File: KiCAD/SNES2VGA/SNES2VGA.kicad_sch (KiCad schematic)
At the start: 16 parts, among them J1 3.5mm_vertical, P1 AVMulti_Main, P2 VGA

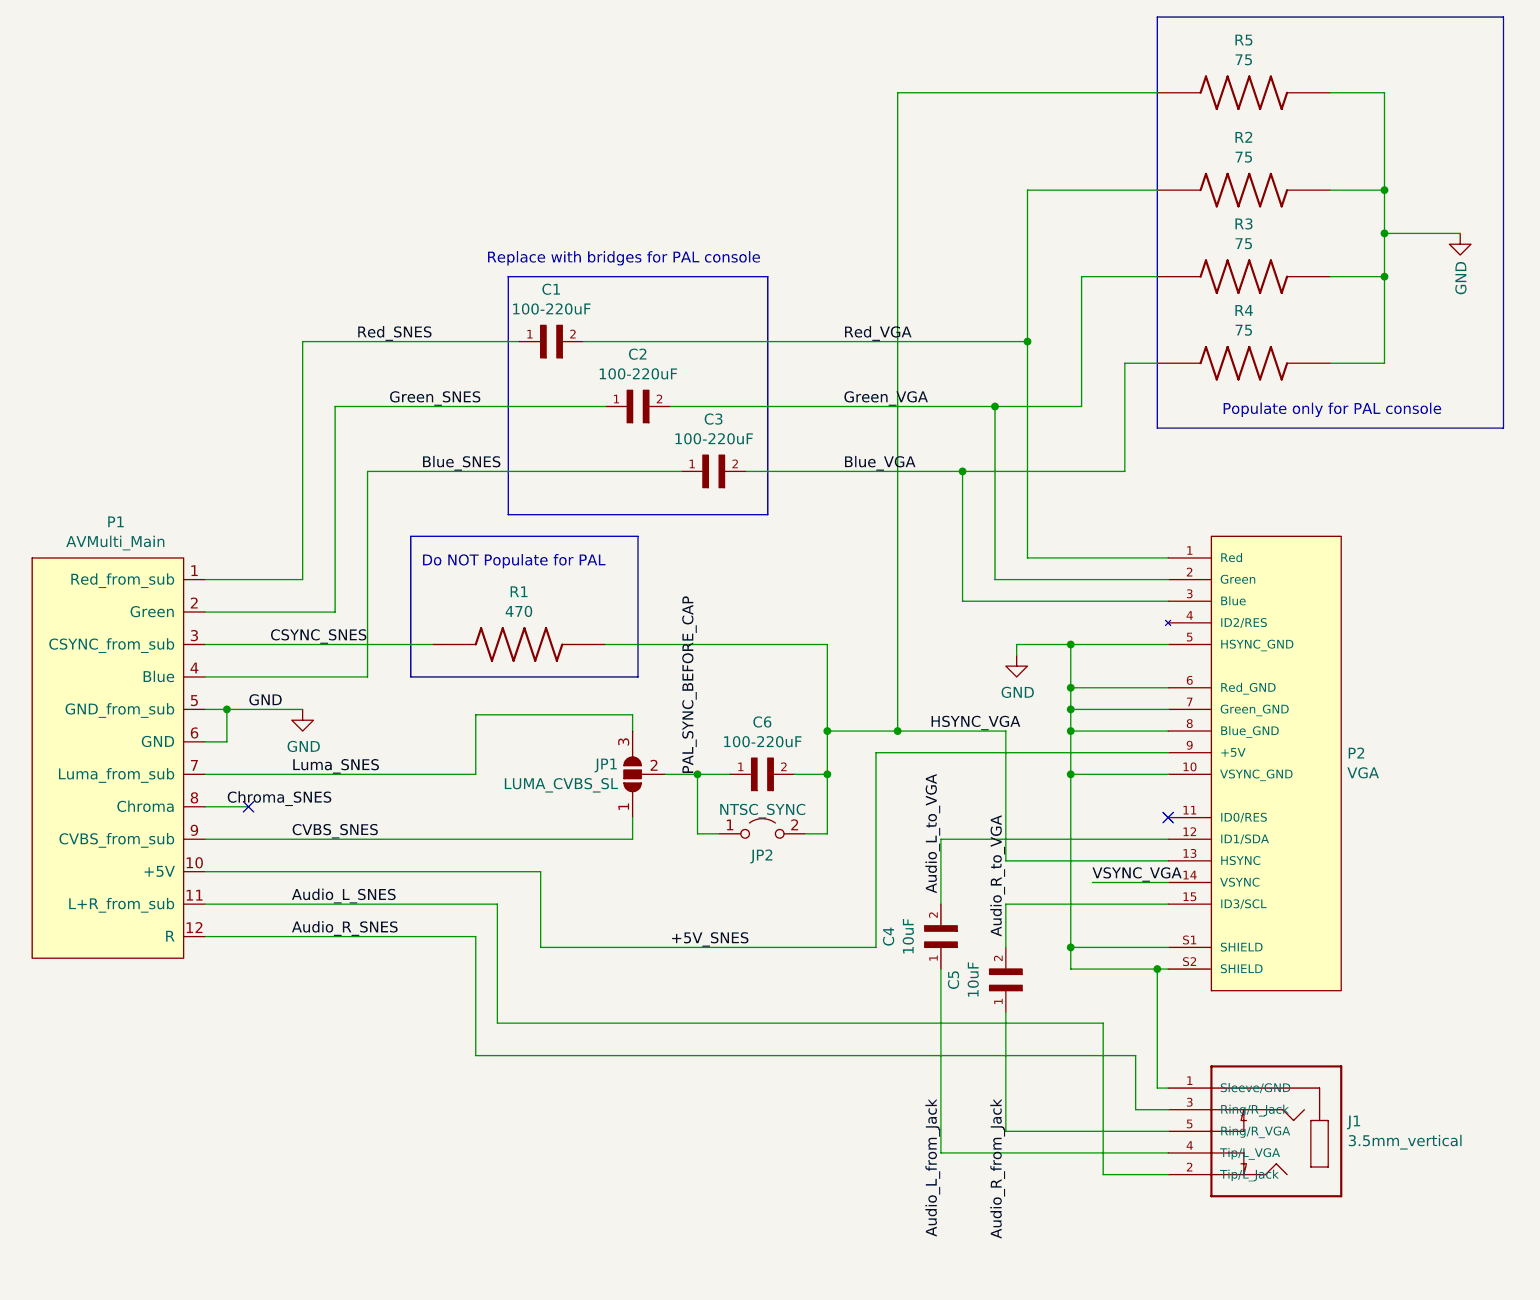
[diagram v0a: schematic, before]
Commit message: Update to KiCad 9
 - Use kicad symbols and footprints if possible
 - Add JLCPCB QR/number placement square/text
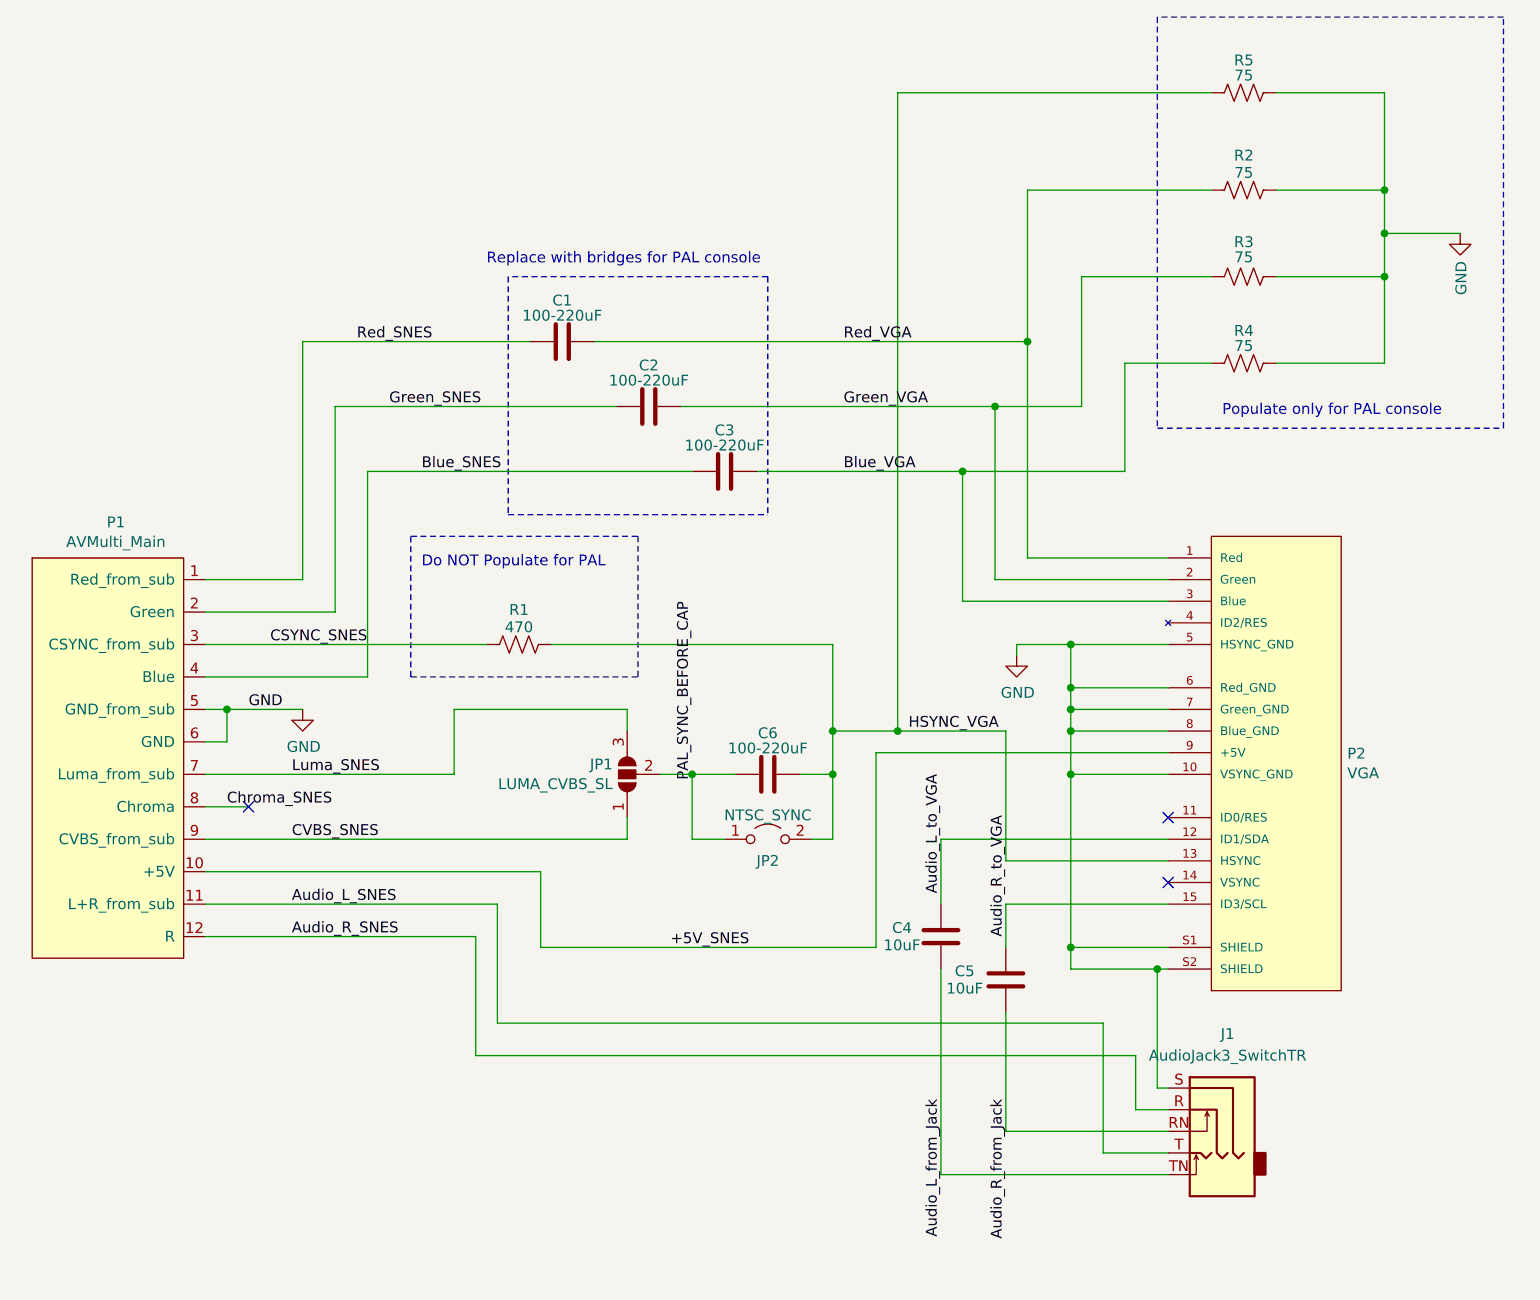
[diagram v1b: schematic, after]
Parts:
- removed J1: 3.5mm_vertical, SNES2VGA_Library:3.5mm_vertical, symbol SNES2VGA_Library:3.5mm_vertical
- added J1: AudioJack3_SwitchTR, Connector_Audio:Jack_3.5mm_CUI_SJ1-3535NG_Horizontal, symbol Connector_Audio:AudioJack3_SwitchTR
- C1, C2, C3, C6: footprint SNES2VGA_Library:Cap_SMD_1206 -> Capacitor_SMD:C_1206_3216Metric; symbol SNES2VGA_Library:Cap_SMD_1206 -> Device:C
- C4, C5: footprint SNES2VGA_Library:Cap_SMD_0603 -> Capacitor_SMD:C_0603_1608Metric; symbol SNES2VGA_Library:Cap_0603 -> Device:C
- JP1: footprint SNES2VGA_Library:SolderJumper-3_P1.3mm_Open_RoundedPad1.0x1.5mm -> Jumper:SolderJumper-3_P1.3mm_Open_RoundedPad1.0x1.5mm; now left out of the parts list
- JP2: now left out of the parts list
- R1, R2, R3, R4, R5: footprint SNES2VGA_Library:Resistor_SMD_0603 -> Resistor_SMD:R_0603_1608Metric; symbol SNES2VGA_Library:Resistor_0603 -> Device:R_US
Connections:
- net Audio_L_SNES: now also J1.T
- net Audio_L_from_Jack: now also C4.2, J1.TN; no longer C4.1
- net Audio_L_to_VGA: now also C4.1; no longer C4.2
- net Audio_R_SNES: now also J1.R
- net Audio_R_from_Jack: now also C5.2, J1.RN; no longer C5.1
- net Audio_R_to_VGA: now also C5.1; no longer C5.2
- net GND: now also J1.S
- net VSYNC_VGA: no longer names the net of P2.14 (VSYNC)
- no-connect marks 2 -> 3
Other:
- moved on the sheet: JP1, JP2

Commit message: Add part information for Digikey and Mfg#
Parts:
- C1, C2, C3, C6: Digikey Product Number (none) -> 490-GRM31CR60J227ME11KCT-ND; Manufacturer Product Number (none) -> GRM31CR60J227ME11K
- C4, C5: Digikey Product Number (none) -> 1276-1119-1-ND; Manufacturer Product Number (none) -> CL10A106MQ8NNNC
- R1: Digikey Product Number (none) -> 311-470HRCT-ND; Manufacturer Product Number (none) -> RC0603FR-07470RL
- R2, R3, R4, R5: Digikey Product Number (none) -> 13-RC0603FR-1075RLCT-ND; Manufacturer Product Number (none) -> RC0603FR-1075RL
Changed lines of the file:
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@@
 			)
 		)
-		(property "Datasheet" "~"
+		(property "Datasheet" "https://mm.digikey.com/Volume0/opasdata/d220001/medias/docus/609/CL10A106MQ8NNNC_Spec.pdf"
 			(at 162.56 121.92 0)
 			(effects
@@
 			)
 		)
+		(property "Digikey Product Number" "1276-1119-1-ND"
+			(at 162.56 121.92 0)
+			(effects
+				(font
+					(size 1.27 1.27)
+				)
+				(hide yes)
+			)
+		)
+		(property "Manufacturer Product Number" "CL10A106MQ8NNNC"
+			(at 162.56 121.92 0)
+			(effects
+				(font
+					(size 1.27 1.27)
+				)
+				(hide yes)
+			)
+		)
 		(pin "1"
 		)
@@
 			)
 		)
-		(property "Datasheet" "~"
+		(property "Datasheet" "https://mm.digikey.com/Volume0/opasdata/d220001/medias/docus/609/CL10A106MQ8NNNC_Spec.pdf"
 			(at 170.18 127 0)
 			(effects
@@
 			)
 		)
+		(property "Digikey Product Number" "1276-1119-1-ND"
+			(at 170.18 127 0)
+			(effects
+				(font
+					(size 1.27 1.27)
+				)
+				(hide yes)
+			)
+		)
+		(property "Manufacturer Product Number" "CL10A106MQ8NNNC"
+			(at 170.18 127 0)
+			(effects
+				(font
+					(size 1.27 1.27)
+				)
+				(hide yes)
+			)
+		)
 		(pin "1"
 		)
@@
 			)
 		)
-		(property "Datasheet" "~"
+		(property "Datasheet" "https://www.yageo.com/upload/media/product/products/datasheet/rchip/PYu-RC_Group_51_RoHS_L_12.pdf"
 			(at 113.03 87.63 0)
 			(effects
@@
 		)
 		(property "Description" "Resistor, US symbol"
+			(at 113.03 87.63 0)
+			(effects
+				(font
+					(size 1.27 1.27)
+				)
+				(hide yes)
+			)
+		)
+		(property "Digikey Product Number" "311-470HRCT-ND"
+			(at 113.03 87.63 0)
+			(effects
+				(font
+					(size 1.27 1.27)
+				)
+				(hide yes)
+			)
+		)
+		(property "Manufacturer Product Number" "RC0603FR-07470RL"
 			(at 113.03 87.63 0)
 			(effects
@@
 			)
 		)
-		(property "Datasheet" "~"
+		(property "Datasheet" "https://search.murata.co.jp/Ceramy/image/img/A01X/G101/ENG/GRM31CR60J227ME11-01A.pdf"
 			(at 118.11 52.07 0)
 			(effects
@@
 		)
 		(property "Description" "Unpolarized capacitor"
+			(at 118.11 52.07 0)
+			(effects
+				(font
+					(size 1.27 1.27)
+				)
+				(hide yes)
+			)
+		)
+		(property "Digikey Product Number" "490-GRM31CR60J227ME11KCT-ND"
+			(at 118.11 52.07 0)
+			(effects
+				(font
+					(size 1.27 1.27)
+				)
+				(hide yes)
+			)
+		)
+		(property "Manufacturer Product Number" "GRM31CR60J227ME11K"
 			(at 118.11 52.07 0)
 			(effects
@@
 			)
 		)
-		(property "Datasheet" "~"
+		(property "Datasheet" "https://search.murata.co.jp/Ceramy/image/img/A01X/G101/ENG/GRM31CR60J227ME11-01A.pdf"
 			(at 128.27 59.69 0)
 			(effects
@@
 		)
 		(property "Description" "Unpolarized capacitor"
+			(at 128.27 59.69 0)
+			(effects
+				(font
+					(size 1.27 1.27)
+				)
+				(hide yes)
+			)
+		)
+		(property "Digikey Product Number" "490-GRM31CR60J227ME11KCT-ND"
+			(at 128.27 59.69 0)
+			(effects
+				(font
+					(size 1.27 1.27)
+				)
+				(hide yes)
+			)
+		)
+		(property "Manufacturer Product Number" "GRM31CR60J227ME11K"
 			(at 128.27 59.69 0)
 			(effects
@@
 			)
 		)
-		(property "Datasheet" "~"
+		(property "Datasheet" "https://search.murata.co.jp/Ceramy/image/img/A01X/G101/ENG/GRM31CR60J227ME11-01A.pdf"
 			(at 137.16 67.31 0)
 			(effects
@@
 			)
 		)
+		(property "Digikey Product Number" "490-GRM31CR60J227ME11KCT-ND"
+			(at 137.16 67.31 0)
+			(effects
+				(font
+					(size 1.27 1.27)
+				)
+				(hide yes)
+			)
+		)
+		(property "Manufacturer Product Number" "GRM31CR60J227ME11K"
+			(at 137.16 67.31 0)
+			(effects
+				(font
+					(size 1.27 1.27)
+				)
+				(hide yes)
+			)
+		)
 		(pin "1"
 		)
@@
 			)
 		)
-		(property "Datasheet" "~"
+		(property "Datasheet" "https://www.yageo.com/upload/media/product/products/datasheet/rchip/PYu-RC_Group_51_RoHS_L_12.pdf"
 			(at 198.12 54.61 0)
 			(effects
@@
 			)
 		)
+		(property "Digikey Product Number" "13-RC0603FR-1075RLCT-ND"
+			(at 198.12 54.61 0)
+			(effects
+				(font
+					(size 1.27 1.27)
+				)
+				(hide yes)
+			)
+		)
+		(property "Manufacturer Product Number" "RC0603FR-1075RL"
+			(at 198.12 54.61 0)
+			(effects
+				(font
+					(size 1.27 1.27)
+				)
+				(hide yes)
+			)
+		)
 		(pin "1"
 		)
@@
 			)
 		)
-		(property "Datasheet" "~"
+		(property "Datasheet" "https://www.yageo.com/upload/media/product/products/datasheet/rchip/PYu-RC_Group_51_RoHS_L_12.pdf"
 			(at 198.12 34.29 0)
 			(effects
@@
 			)
 		)
+		(property "Digikey Product Number" "13-RC0603FR-1075RLCT-ND"
+			(at 198.12 34.29 0)
+			(effects
+				(font
+					(size 1.27 1.27)
+				)
+				(hide yes)
+			)
+		)
+		(property "Manufacturer Product Number" "RC0603FR-1075RL"
+			(at 198.12 34.29 0)
+			(effects
+				(font
+					(size 1.27 1.27)
+				)
+				(hide yes)
+			)
+		)
 		(pin "1"
 		)
@@
 			)
 		)
-		(property "Datasheet" "~"
+		(property "Datasheet" "https://www.yageo.com/upload/media/product/products/datasheet/rchip/PYu-RC_Group_51_RoHS_L_12.pdf"
 			(at 198.12 44.45 0)
 			(effects
@@
 			)
 		)
+		(property "Digikey Product Number" "13-RC0603FR-1075RLCT-ND"
+			(at 198.12 44.45 0)
+			(effects
+				(font
+					(size 1.27 1.27)
+				)
+				(hide yes)
+			)
+		)
+		(property "Manufacturer Product Number" "RC0603FR-1075RL"
+			(at 198.12 44.45 0)
+			(effects
+				(font
+					(size 1.27 1.27)
+				)
+				(hide yes)
+			)
+		)
 		(pin "1"
 		)
@@
 			)
 		)
-		(property "Datasheet" "~"
+		(property "Datasheet" "https://www.yageo.com/upload/media/product/products/datasheet/rchip/PYu-RC_Group_51_RoHS_L_12.pdf"
 			(at 198.12 22.86 0)
 			(effects
@@
 		)
 		(property "Description" "Resistor, US symbol"
+			(at 198.12 22.86 0)
+			(effects
+				(font
+					(size 1.27 1.27)
+				)
+				(hide yes)
+			)
+		)
+		(property "Digikey Product Number" "13-RC0603FR-1075RLCT-ND"
+			(at 198.12 22.86 0)
+			(effects
+				(font
+					(size 1.27 1.27)
+				)
+				(hide yes)
+			)
+		)
+		(property "Manufacturer Product Number" "RC0603FR-1075RL"
 			(at 198.12 22.86 0)
 			(effects
@@
 			)
 		)
-		(property "Datasheet" "~"
+		(property "Datasheet" "https://search.murata.co.jp/Ceramy/image/img/A01X/G101/ENG/GRM31CR60J227ME11-01A.pdf"
 			(at 142.24 102.87 0)
 			(effects
@@
 			(at 142.24 102.87 0)
 			(effects
+				(font
+					(size 1.27 1.27)
+				)
+				(hide yes)
+			)
+		)
+		(property "Digikey Product Number" "490-GRM31CR60J227ME11KCT-ND"
+			(at 142.24 102.87 0)
+			(effects
+				(font
+					(size 1.27 1.27)
+				)
+				(hide yes)
+			)
+		)
+		(property "Manufacturer Product Number" "GRM31CR60J227ME11K"
+			(at 142.24 102.87 0)
+			(effects
